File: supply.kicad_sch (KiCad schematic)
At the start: 66 parts, among them J17 JST_SH_1x2_BM02B-SRSS-TB-LF-SN, J7 BarrelJack_Pin1.3mm_694103107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, J8 JST_SH_1x4_BM04B-SRSS-TB-LF-SN, Q12 SI7613DN-T1-GE3, Q13 SI7613DN-T1-GE3, Q14 BSS138PW, Q15 BSS138PW, Q16 BSS138PW, Q17 BSS138PW, Q28 BSS138PW, Q29 SI7613DN-T1-GE3, SW4 SW_CVS-08TB, SW5 SW_KMR211NGLFS_SMD, U17 LTC4412IS6, U18 LTC4412IS6, U21 NCP718BSN330T1G, U22 MAX16150A_SOT, U26 MAX812REUS+T, U29 AT24CS01_SOT23, U31 LM3880

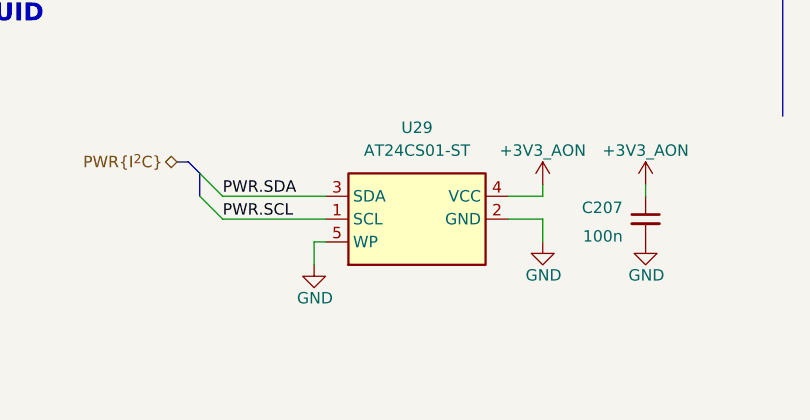
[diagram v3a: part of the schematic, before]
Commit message: [#69798] Fix I2C adresses descriptions on the schematic
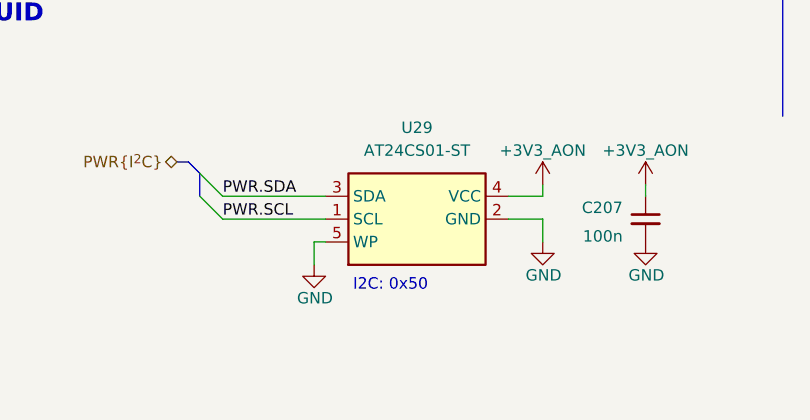
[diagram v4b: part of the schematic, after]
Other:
- note added: "I2C: 0x50"
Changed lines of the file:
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@@
+		)
+	)
+	(text "I2C: 0x50"
+		(exclude_from_sim no)
+		(at 251.968 272.288 0)
+		(effects
+			(font
+				(size 1.27 1.27)
+			)
+			(justify left bottom)
 		)
 	)

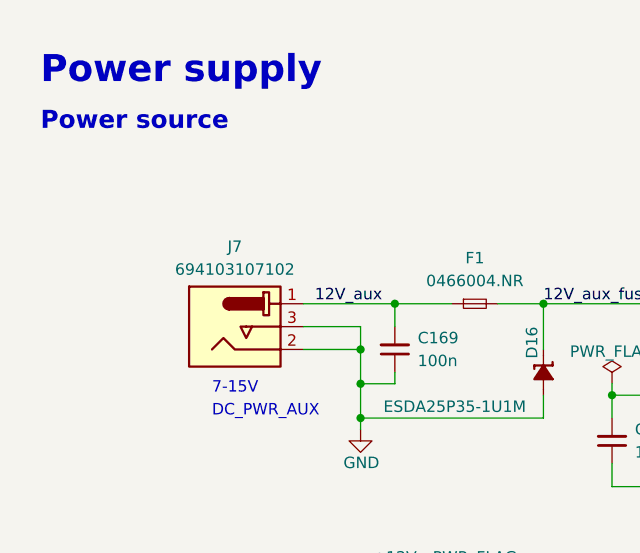
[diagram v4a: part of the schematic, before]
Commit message: [#69493] Replace DC input power connector
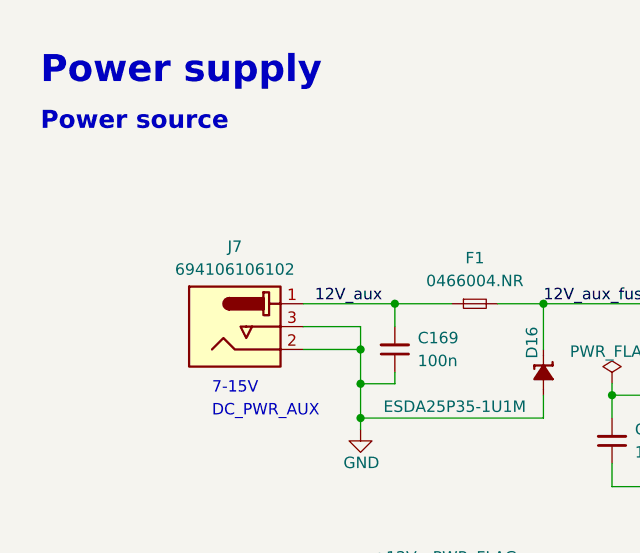
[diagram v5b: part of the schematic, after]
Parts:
- removed J7: BarrelJack_Pin1.3mm_694103107102, antmicro-footprints:BarrelJack_Pin1.3mm_694103107102, symbol antmicroBarrelPowerConnectors:BarrelJack_Pin1.3mm_694103107102
- added J7: BarrelJack_Pin2mm_694106106102, antmicro-footprints:BarrelJack_Pin2mm_694106106102, symbol antmicroBarrelPowerConnectors:BarrelJack_Pin2mm_694106106102
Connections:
- net 12V_aux: now also J7.1
- net GND: now also J7.2, J7.3
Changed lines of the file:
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@@
 	)
 	(symbol
+		(lib_id "antmicroBarrelPowerConnectors:BarrelJack_Pin2mm_694106106102")
+		(at 43.18 44.45 0)
+		(unit 1)
+		(exclude_from_sim no)
+		(in_bom yes)
+		(on_board yes)
+		(dnp no)
+		(fields_autoplaced yes)
+		(property "Reference" "J7"
+			(at 35.56 38.1 0)
+			(effects
+				(font
+					(size 1.27 1.27)
+					(thickness 0.15)
+				)
+			)
+		)
+		(property "Value" "BarrelJack_Pin2mm_694106106102"
+			(at 58.42 54.61 0)
+			(effects
+				(font
+					(size 1.27 1.27)
+					(thickness 0.15)
+				)
+				(justify left bottom)
+				(hide yes)
+			)
+		)
+		(property "Footprint" "antmicro-footprints:BarrelJack_Pin2mm_694106106102"
+			(at 58.42 57.15 0)
+			(effects
+				(font
+					(size 1.27 1.27)
+					(thickness 0.15)
+				)
+				(justify left bottom)
+				(hide yes)
+			)
+		)
+		(property "Datasheet" "https://www.we-online.com/components/products/datasheet/694106106102.pdf"
+			(at 58.42 59.69 0)
+			(effects
+				(font
+					(size 1.27 1.27)
+					(thickness 0.15)
+				)
+				(justify left bottom)
+				(hide yes)
+			)
+		)
+		(property "Description" "DC Power Connector, Jack, 5 A, 2 mm, PCB Mount, Surface Mount"
+			(at 58.42 62.23 0)
+			(effects
+				(font
+					(size 1.27 1.27)
+					(thickness 0.15)
+				)
+				(justify left bottom)
+				(hide yes)
+			)
+		)
+		(property "MPN" "694106106102"
+			(at 35.56 40.64 0)
+			(effects
+				(font
+					(size 1.27 1.27)
+					(thickness 0.15)
+				)
+			)
+		)
+		(property "Manufacturer" "Würth Elektronik"
+			(at 58.42 64.77 0)
+			(effects
+				(font
+					(size 1.27 1.27)
+					(thickness 0.15)
+				)
+				(justify left bottom)
+				(hide yes)
+			)
+		)
+		(property "Author" "Antmicro"
+			(at 58.42 67.31 0)
+			(effects
+				(font
+					(size 1.27 1.27)
+					(thickness 0.15)
+				)
+				(justify left bottom)
+				(hide yes)
+			)
+		)
+		(property "License" "Apache-2.0"
+			(at 58.42 69.85 0)
+			(effects
+				(font
+					(size 1.27 1.27)
+					(thickness 0.15)
+				)
+				(justify left bottom)
+				(hide yes)
+			)
+		)
+		(pin "2"
+		)
+		(pin "3"
+		)
+		(pin "1"
+		)
+		(pin "1"
+		)
+		(instances
+			(project ""
+				(path "/1faa6543-e26a-4449-8bac-ee14b9f19e5f/00000000-0000-0000-0000-000060225b0c"
+					(reference "J7")
+					(unit 1)
+				)
+			)
+		)
+	)
+	(symbol
 		(lib_id "antmicroResistors0402:R_4k7_0402")
 		(at 229.87 175.26 90)
@@
 					(unit 1)
 				)
-			)
-		)
-	)
-	(symbol
-		(lib_id "antmicroBarrelPowerConnectors:BarrelJack_Pin1.3mm_694103107102")
-		(at 43.18 44.45 0)
-		(unit 1)
-		(exclude_from_sim no)
-		(in_bom yes)
-		(on_board yes)
-		(dnp no)
-		(fields_autoplaced yes)
-		(property "Reference" "J7"
-			(at 35.56 38.1 0)
-			(effects
-				(font
-					(size 1.27 1.27)
-					(thickness 0.15)
-				)
-			)
-		)
-		(property "Value" "BarrelJack_Pin1.3mm_694103107102"
-			(at 58.42 57.15 0)
-			(effects
-				(font
-					(size 1.27 1.27)
-					(thickness 0.15)
-				)
-				(justify left bottom)
-				(hide yes)
-			)
-		)
-		(property "Footprint" "antmicro-footprints:BarrelJack_Pin1.3mm_694103107102"
-			(at 58.42 59.69 0)
-			(effects
-				(font
-					(size 1.27 1.27)
-					(thickness 0.15)
-				)
-				(justify left bottom)
-				(hide yes)
-			)
-		)
-		(property "Datasheet" "https://www.we-online.de/katalog/datasheet/694103107102.pdf"
-			(at 58.42 62.23 0)
-			(effects
-				(font
-					(size 1.27 1.27)
-					(thickness 0.15)
-				)
-				(justify left bottom)
-				(hide yes)
-			)
-		)
-		(property "Description" ""
-			(at 43.18 44.45 0)
-			(effects
-				(font
-					(size 1.27 1.27)
-				)
-				(hide yes)
-			)
-		)
-		(property "MPN" "694103107102"
-			(at 35.56 40.64 0)
-			(effects
-				(font
-					(size 1.27 1.27)
-					(thickness 0.15)
-				)
-			)
-		)
-		(property "Manufacturer" "Würth Elektronik"
-			(at 58.42 64.77 0)
-			(effects
-				(font
-					(size 1.27 1.27)
-					(thickness 0.15)
-				)
-				(justify left bottom)
-				(hide yes)
-			)
-		)
-		(property "Author" "Antmicro"
-			(at 58.42 67.31 0)
-			(effects
-				(font
-					(size 1.27 1.27)
-					(thickness 0.15)
-				)
-				(justify left bottom)
-				(hide yes)
-			)
-		)
-		(property "License" "Apache-2.0"
-			(at 58.42 69.85 0)
-			(effects
-				(font
-					(size 1.27 1.27)
-					(thickness 0.15)
-				)
-				(justify left bottom)
-				(hide yes)
-			)
-		)
-		(pin "3"
-		)
-		(pin "1"
-		)
-		(pin "1"
-		)
-		(pin "2"
-		)
-		(instances
-			(project "data-center-rdimm-ddr5-tester"
-				(path "/1faa6543-e26a-4449-8bac-ee14b9f19e5f/00000000-0000-0000-0000-000060225b0c"
-					(reference "J7")
-					(unit 1)
-				)

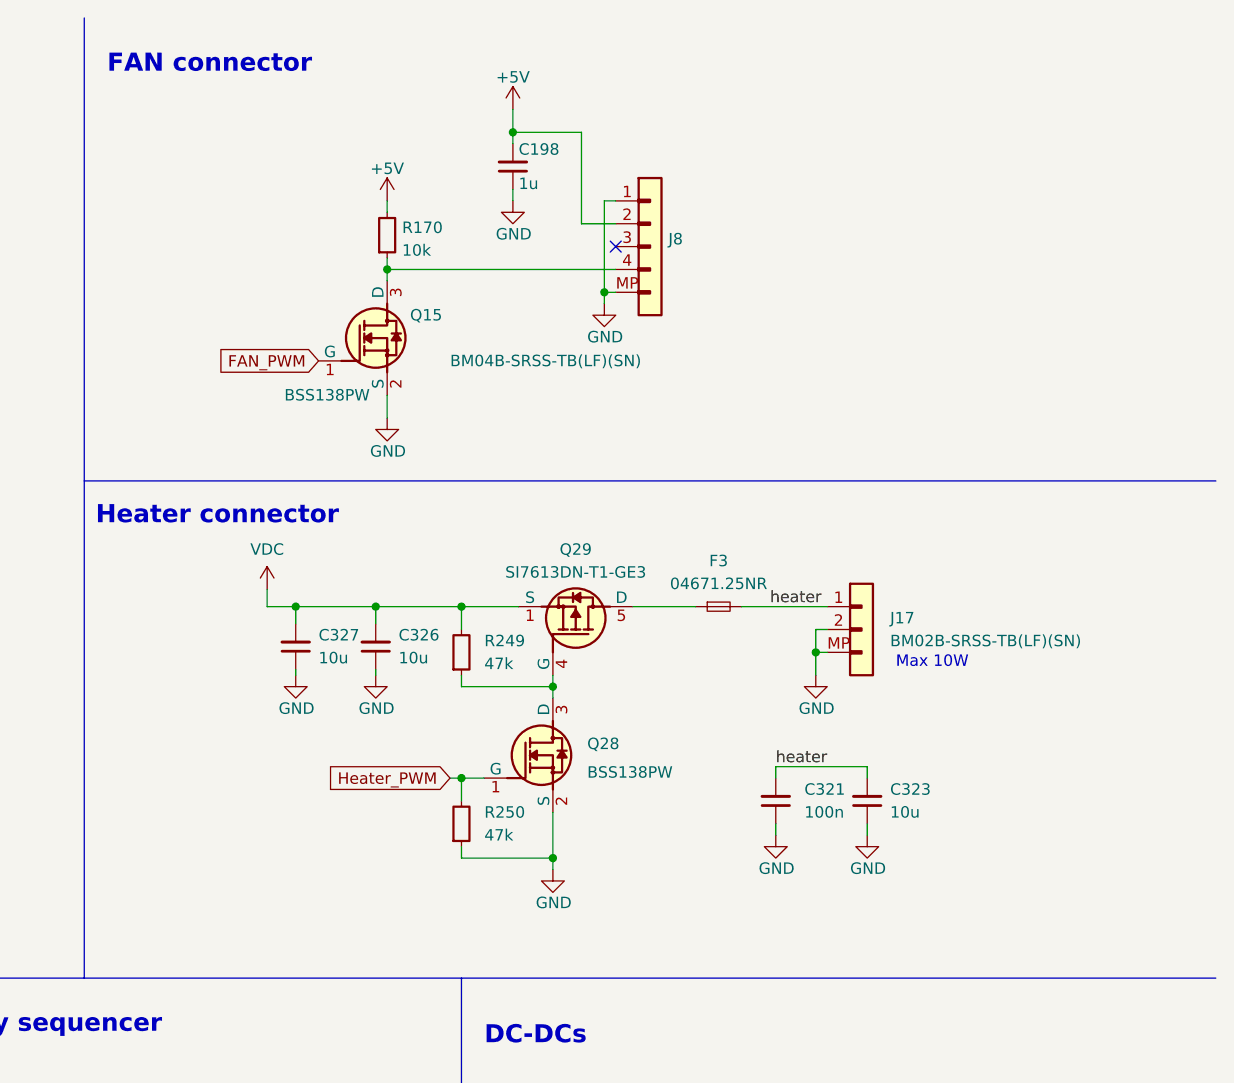
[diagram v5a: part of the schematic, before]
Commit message: [#70506] Clean DRC and ERC
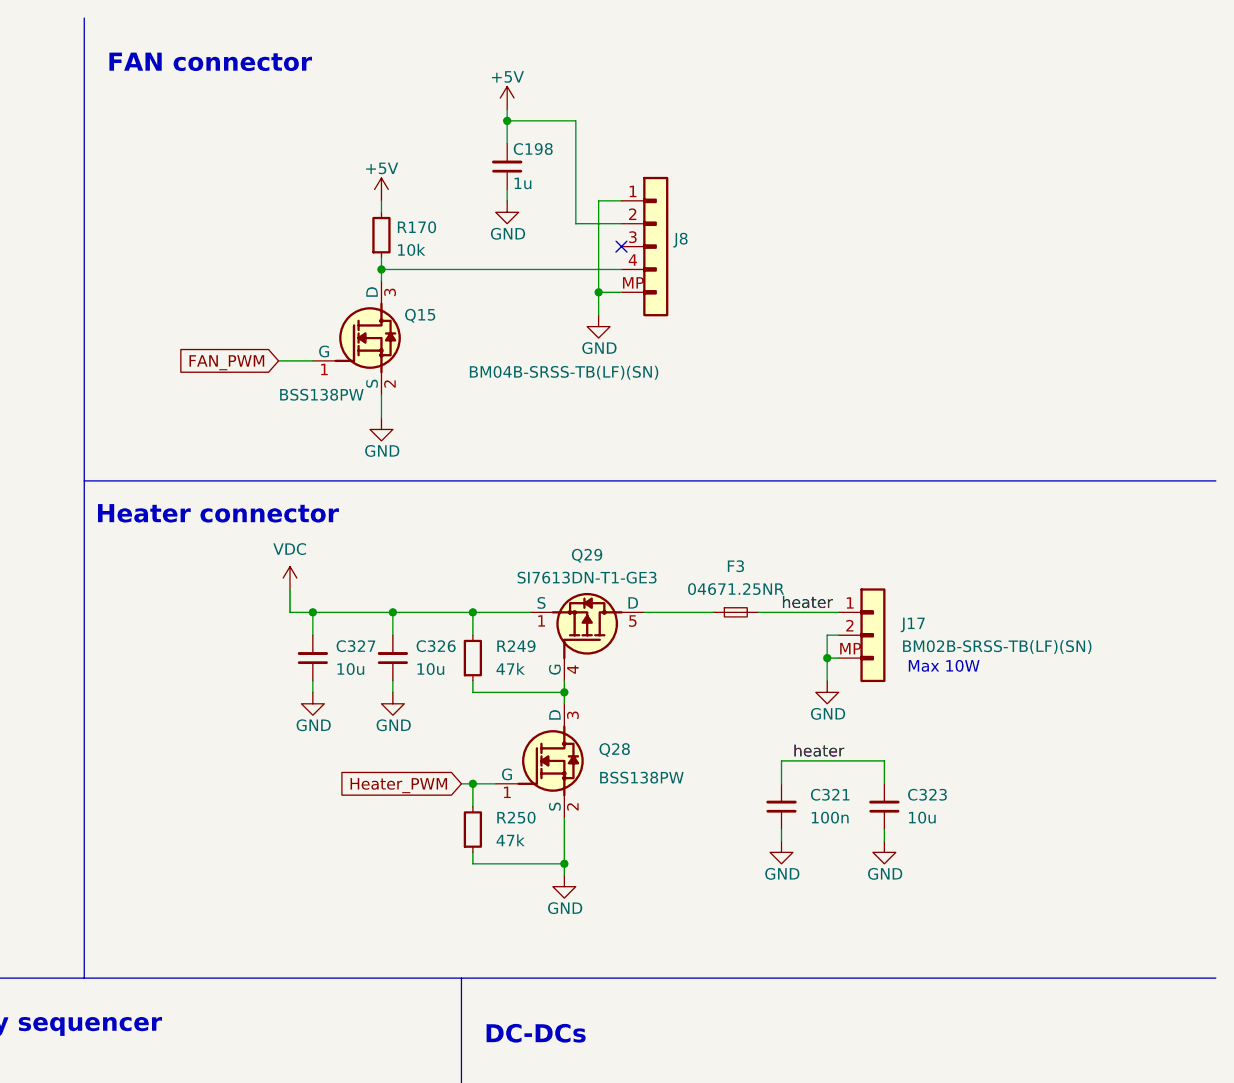
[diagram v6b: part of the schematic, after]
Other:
- moved on the sheet: C198, C321, C323, C326, C327, F3, J17, J8, Q15, Q28, Q29, R170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
